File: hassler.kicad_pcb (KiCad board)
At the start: 2 copper layers, 59 parts, among them CON1 USB-MICRO-B, J1 JST, Q1 IRF510, Q2 IRF510, Q3 MMBT2222A, SW1 Off Switcher, U1 TL082, U2 TL081, U3 MCP73831, U4 LT1308

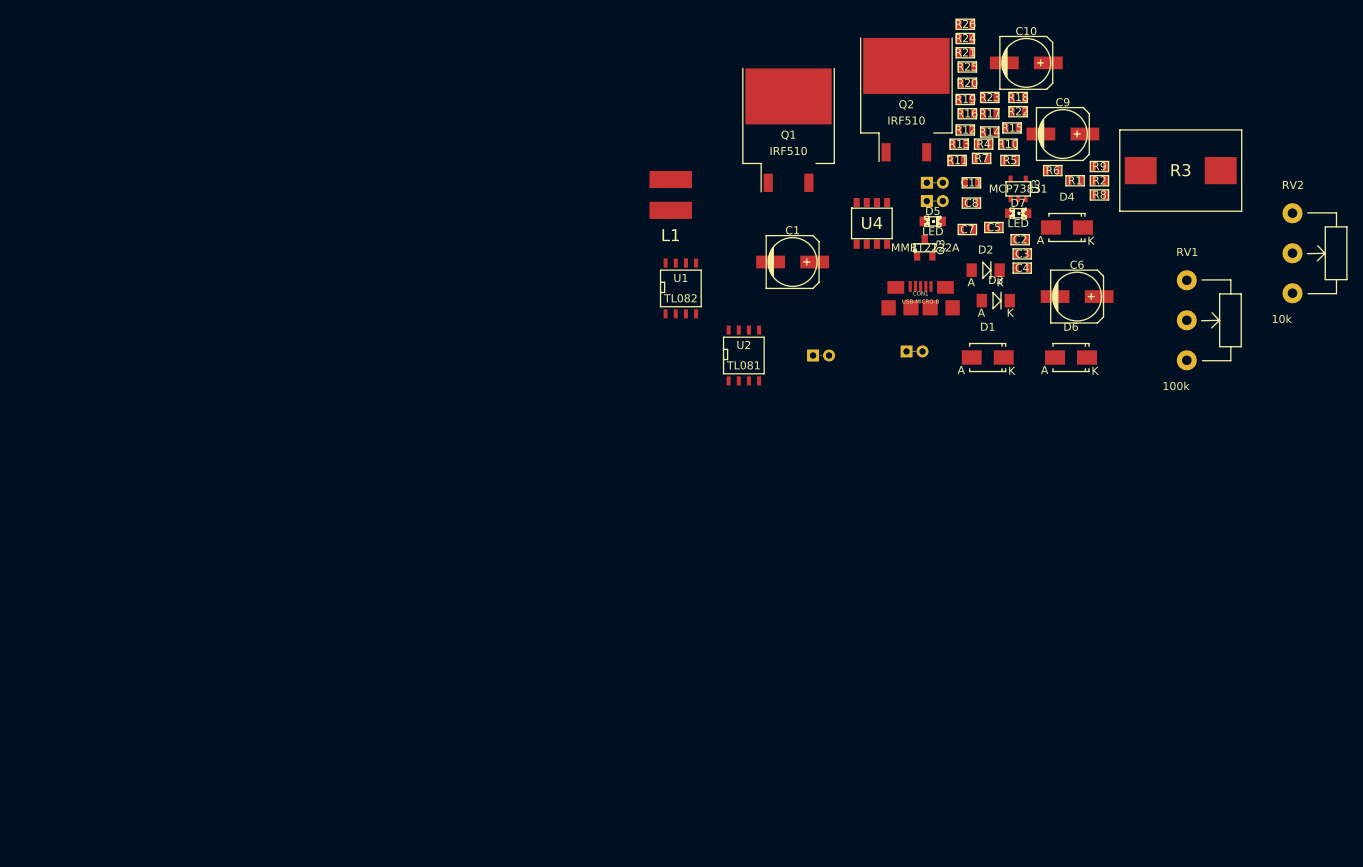
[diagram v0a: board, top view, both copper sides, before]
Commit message: Layout lipo recharge circuit
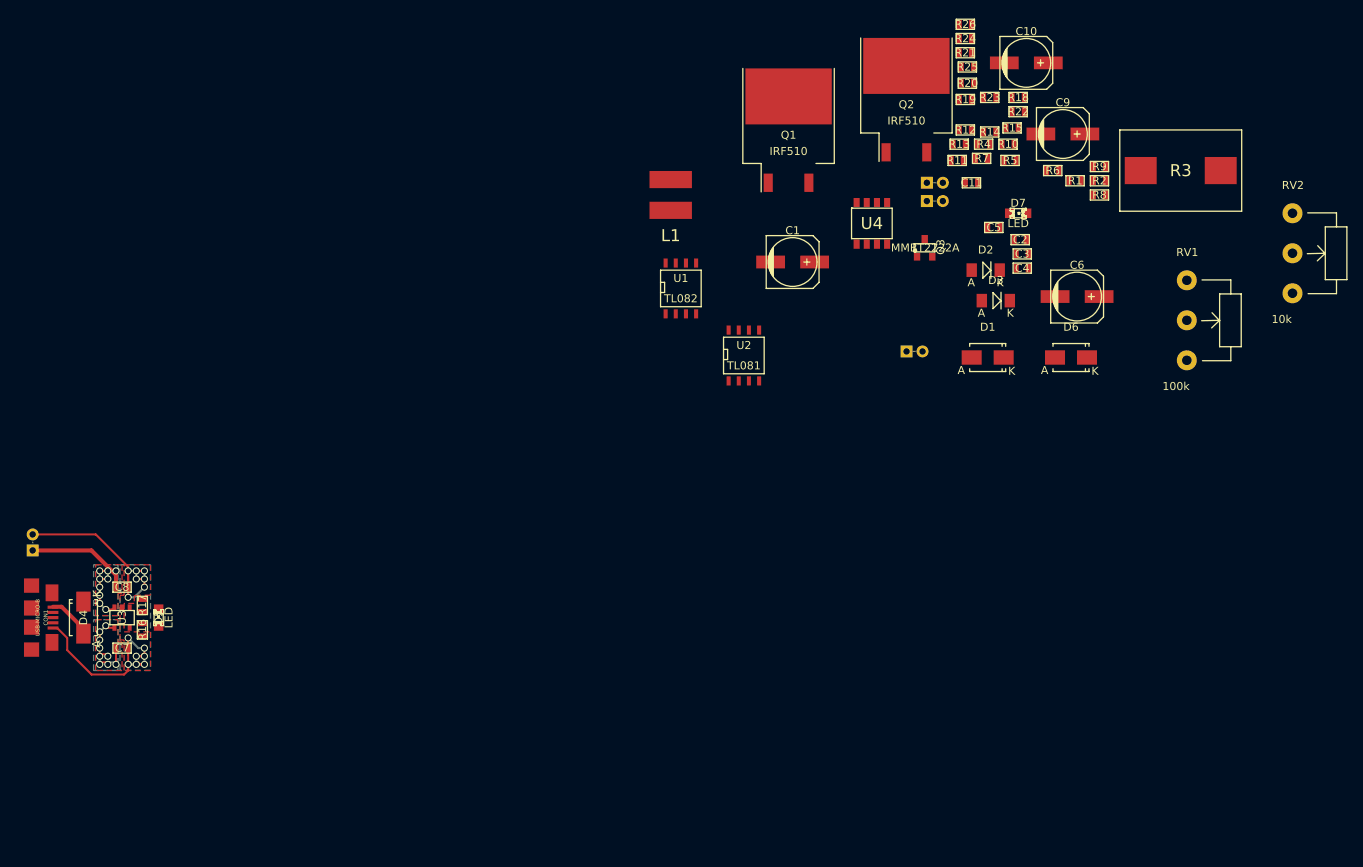
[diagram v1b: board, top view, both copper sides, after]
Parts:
- moved D4 132.3 mm to (106.7, 97.0), turned to 90 degrees
- moved U3 124.2 mm to (111.5, 97.0), turned to 180 degrees
- moved R17 122.5 mm to (114.0, 95.5), turned to 90 degrees
- moved R16 121.6 mm to (114.0, 98.6), turned to 270 degrees
- moved C7 117.9 mm to (111.5, 100.8)
- moved C8 116.5 mm to (111.5, 93.2)
- moved CON1 116.1 mm to (102.9, 97.0), turned to 270 degrees
- moved D5 108.7 mm to (116.1, 97.0), turned to 90 degrees
- moved J1 101.3 mm to (100.3, 87.6), turned to 90 degrees
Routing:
- net GND: track 0.00 -> 56.6 mm, vias 0 -> 14
- net +BATT: track 0.00 -> 25.6 mm, vias 0 -> 9
- net Net-(C7-Pad1): track 0.00 -> 11.2 mm, vias 0 -> 9
- net Net-(CON1-Pad1): track 0.00 -> 5.57 mm
- added copper zone on B.Cu, net +BATT
- added copper zone on F.Cu, net +BATT
- added copper zone on B.Cu, net GND
- added copper zone on F.Cu, net GND
- added copper zone on B.Cu, net Net-(C7-Pad1)
- added copper zone on F.Cu, net Net-(C7-Pad1)
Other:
- net class Power added: clearance 0.254, trace_width 0.508, via_dia 0.889, via_drill 0.635

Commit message: Layout boost circuit
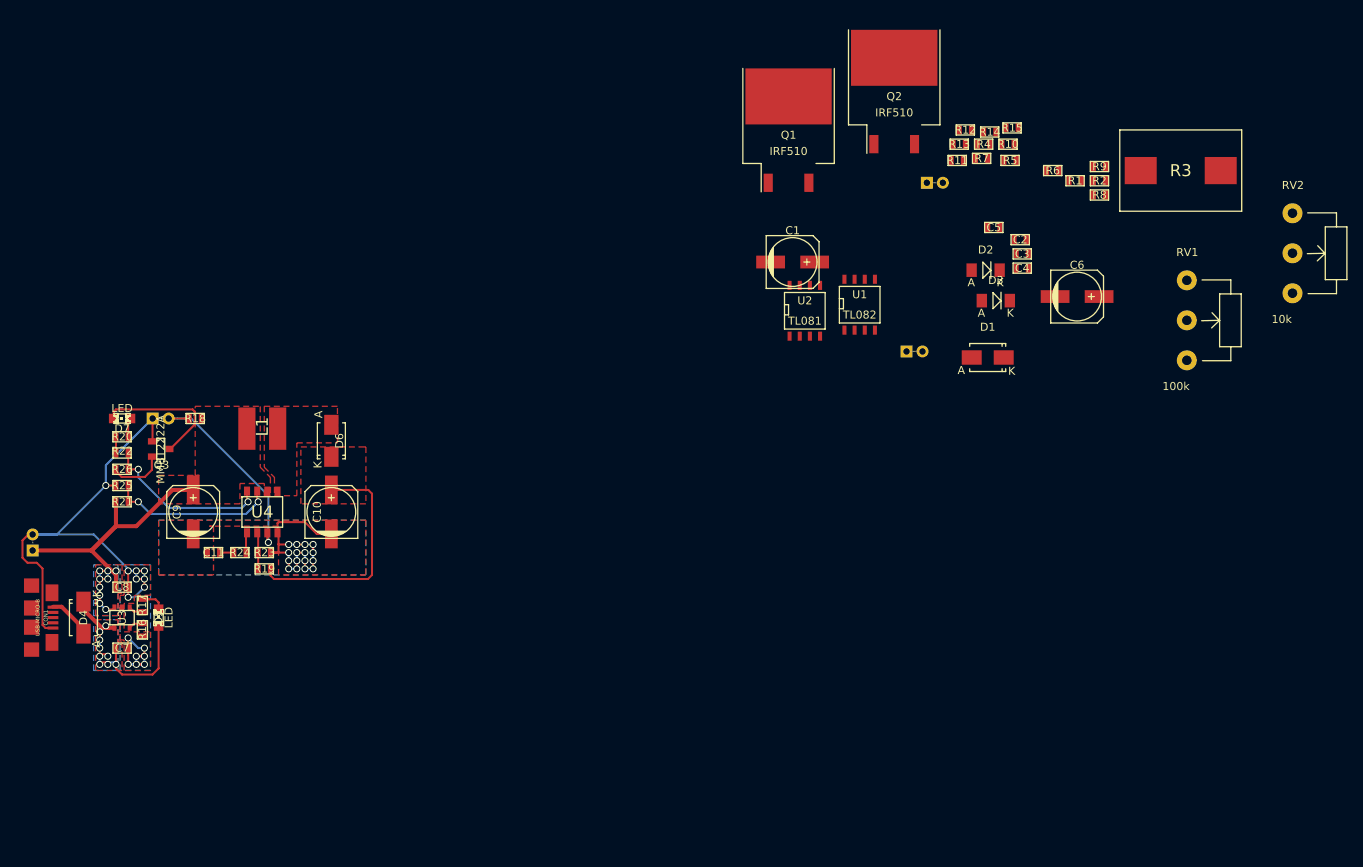
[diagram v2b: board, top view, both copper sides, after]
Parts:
- moved R22 119.9 mm to (111.5, 76.5)
- moved R21 119.4 mm to (111.5, 82.5)
- moved R26 119.2 mm to (111.5, 78.5)
- moved C9 118.5 mm to (120.4, 83.8), turned to 90 degrees
- moved R25 117.9 mm to (111.5, 80.5), turned to 180 degrees
- moved D7 114.9 mm to (111.5, 72.1), turned to 180 degrees
- moved R20 114.5 mm to (111.5, 74.4)
- moved R24 111.1 mm to (126.2, 88.9), turned to 180 degrees
- moved R18 110.4 mm to (120.7, 72.1), turned to 180 degrees
- moved R23 107.0 mm to (129.3, 88.9)
- moved R19 105.5 mm to (129.3, 90.9), turned to 180 degrees
- moved C11 105.4 mm to (122.9, 88.9), turned to 180 degrees
- moved C10 103.4 mm to (137.7, 83.8), turned to 90 degrees
- moved SW1 100.5 mm to (116.3, 72.1)
- moved Q3 98.8 mm to (116.3, 75.9), turned to 270 degrees
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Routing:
- net GND: track 56.6 -> 114.7 mm, vias 14 -> 31
- net VCC: track 0.00 -> 31.4 mm
- net Net-(R18-Pad2): track 0.00 -> 26.1 mm, vias 0 -> 1
- net +BATT: track 25.6 -> 48.8 mm
- net LB_OUT: track 0.00 -> 21.3 mm, vias 0 -> 2
- net LB_IN: track 0.00 -> 20.9 mm, vias 0 -> 2
- net Net-(C7-Pad1): track 11.2 -> 30.8 mm
- net Net-(D7-Pad2): track 0.00 -> 17.3 mm
- net Net-(Q3-Pad2): track 0.00 -> 7.06 mm
- net Net-(R19-Pad2): track 0.00 -> 4.56 mm
- net Net-(D5-Pad2): track 0.00 -> 3.04 mm
- net Net-(R24-Pad1): track 0.00 -> 2.53 mm
- net Net-(D7-Pad1): track 0.00 -> 2.40 mm
- net Net-(R17-Pad1): track 0.00 -> 1.80 mm
- net Net-(R16-Pad1): track 0.00 -> 1.80 mm
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- added copper zone on F.Cu, net Net-(D6-Pad1)
- added copper zone on F.Cu, net VCC

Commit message: Finish PCB layout
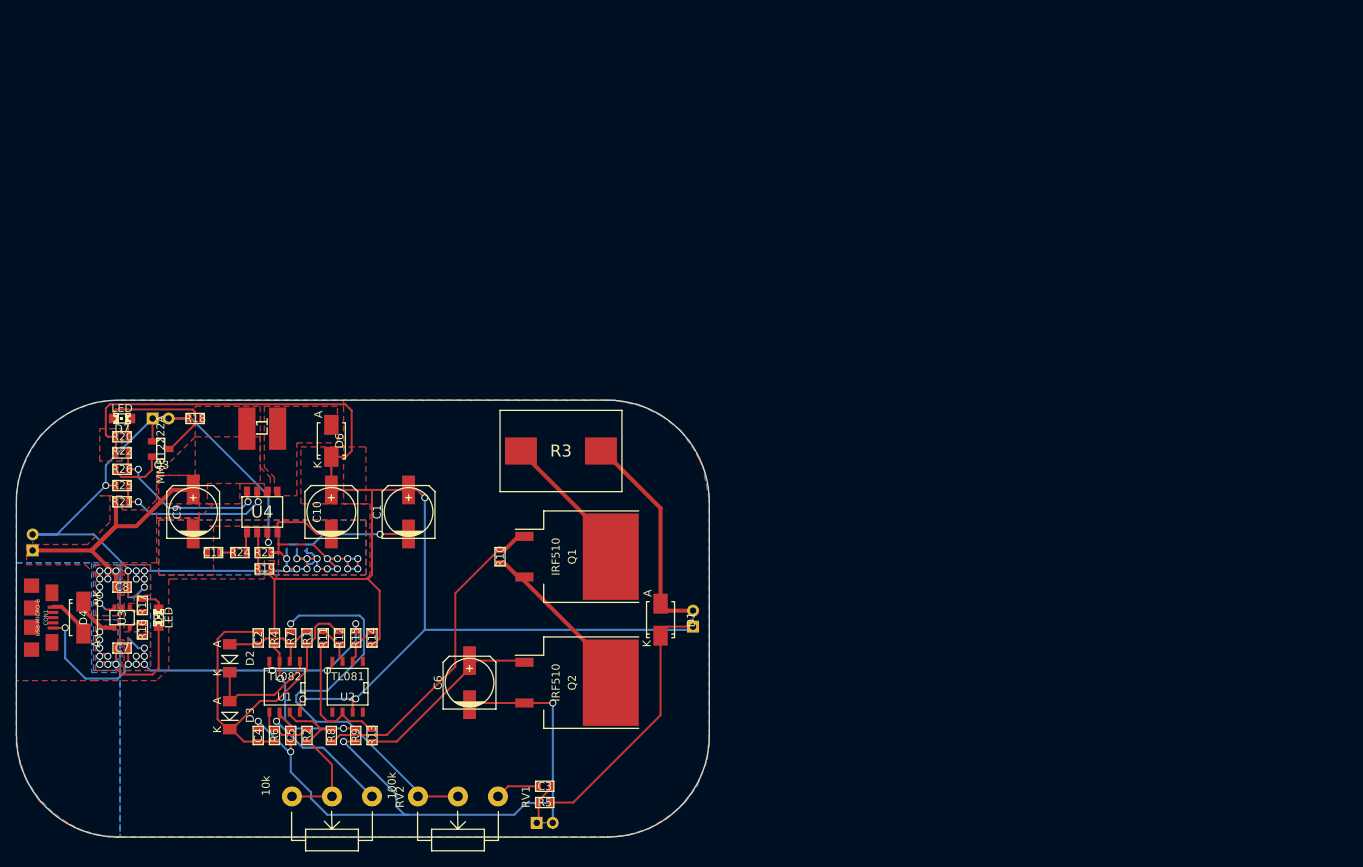
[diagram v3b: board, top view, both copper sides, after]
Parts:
- moved RV2 136.2 mm to (142.7, 119.4), turned to 270 degrees
- moved R2 120.9 mm to (134.6, 111.8), turned to 90 degrees
- moved R6 120.2 mm to (130.6, 111.8), turned to 270 degrees
- moved R8 117.4 mm to (137.7, 111.8), turned to 90 degrees
- moved R9 117.0 mm to (140.7, 111.8), turned to 90 degrees
- moved C4 112.0 mm to (128.5, 111.8), turned to 90 degrees
- moved R1 111.7 mm to (134.6, 99.6), turned to 90 degrees
- moved D3 108.9 mm to (125.0, 109.2), turned to 270 degrees
- moved C5 108.4 mm to (132.6, 111.8), turned to 270 degrees
- moved R4 108.0 mm to (130.6, 99.6), turned to 90 degrees
- moved RV1 107.6 mm to (158.5, 119.4), turned to 270 degrees
- moved C2 107.5 mm to (128.5, 99.6), turned to 270 degrees
- moved D2 106.2 mm to (125.0, 102.1), turned to 270 degrees
- moved R7 105.1 mm to (132.6, 99.6), turned to 90 degrees
- moved R13 104.2 mm to (142.7, 111.8), turned to 90 degrees
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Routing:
- net VCC: track 31.4 -> 213.1 mm, vias 0 -> 3
- net GND: track 114.7 -> 285.7 mm, vias 31 -> 38
- net Net-(R7-Pad2): track 0.00 -> 52.0 mm, vias 0 -> 1
- net Net-(C2-Pad1): track 0.00 -> 46.1 mm
- net Net-(Q1-Pad1): track 0.00 -> 40.7 mm
- net Net-(D1-Pad1): track 0.00 -> 27.9 mm
- net Net-(C6-Pad1): track 0.00 -> 23.9 mm
- net Net-(Q1-Pad3): track 0.00 -> 22.0 mm
- net Net-(R2-Pad1): track 0.00 -> 21.7 mm
- net Net-(C5-Pad1): track 0.00 -> 20.4 mm, vias 0 -> 1
- net Net-(R4-Pad1): track 0.00 -> 19.3 mm, vias 0 -> 2
- net Net-(Q1-Pad2): track 0.00 -> 17.9 mm
- net Net-(R11-Pad1): track 0.00 -> 17.3 mm
- net Net-(D2-Pad2): track 0.00 -> 15.0 mm
- net Net-(C2-Pad2): track 0.00 -> 13.1 mm
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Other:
- board outline added: 86.6 x 54.6 mm
